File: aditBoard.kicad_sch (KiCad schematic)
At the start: 36 parts, among them J1 USB_C_Receptacle_USB2.0, J2 Hashboard0, U2 W25X40CLUXIG TR, U3 RP2040, U4 RT9080-33GJ5, Y1 12MHz

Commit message: pretty much routed
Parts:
- removed R24, R26, R28: 4.7K, Resistor_SMD:R_0805_2012Metric, symbol Device:R_US
- added R1: 10k, Resistor_SMD:R_0402_1005Metric, symbol Device:R_US
- J2: footprint Connector_PinHeader_2.00mm:PinHeader_2x09_P2.00mm_Horizontal -> aditBoard:PinHeader_2x09_P2.00mm_Horizontal
- R25, R27, R29: footprint Resistor_SMD:R_0805_2012Metric -> Resistor_SMD:R_0402_1005Metric
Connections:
- net PLUG0 is gone; now on net PLUG: J2.5 (Pin_5)
- net RST0 is gone; now on net RST: J2.15 (Pin_15)
- net SCL0 is gone; now on net SCL: J2.4 (Pin_4)
- net SDA0 is gone; now on net SDA: J2.3 (Pin_3)
- net UART_RX is gone; now on net RXD: U3.12 (GPIO9)
- net UART_TX is gone; now on net TXD: U3.11 (GPIO8)
- net 3V3: now also R1.1
- net QSPI_SS: now also R1.2
- net PLUG: now reaches U3.13 (GPIO10)
- net RST: now reaches U3.14 (GPIO11)
- net A00 renamed A0
- net A10 renamed A1
- net A20 renamed A2
- net I2C_SCL renamed SCL
- net I2C_SDA renamed SDA
- net POWERUP: no longer names the net of U3.8 (GPIO6)
- net RXD0 renamed RXD
- net TXD0 renamed TXD
- no-connect marks 14 -> 28
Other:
- moved on the sheet: R27, R29, TP1, TP6

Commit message: added artwork, DRC, LCSC BOM
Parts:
- removed TP1, TP4, TP5, TP6: TestPoint, TestPoint:TestPoint_Pad_D1.0mm, symbol Connector:TestPoint
- C17, C18: LCSC Part (none) -> C52923
- J1: LCSC Part (none) -> C2988369
- J2: LCSC C3012192 -> (none); LCSC Part (none) -> C3012192
- R1: LCSC Part (none) -> C25744
- R25, R27, R29: LCSC Part (none) -> C25900
- R4, R5: LCSC Part (none) -> C25905
- U3: LCSC Part (none) -> C2040
- U4: value RT9080-33GJ5 -> AP2112K-3.3TRG1; footprint aditBoard:RT9080-33GJ5 -> aditBoard:SOT-25-5_L2.9-W1.6-P0.95-LS2.8-BL; symbol aditBoard:RT9080-33GJ5 -> aditBoard:AP2112K-3.3TRG1; DK 1028-1509-1-ND -> (none); LCSC Part (none) -> C51118; PARTNO RT9080-33GJ5 -> (none)
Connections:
- net SWCLK: now reaches U3.24 (SWCLK)
- net SWCLK: now also J1.A8 (SBU1)
- net SWD: now reaches U3.25 (SWD)
- net SWD: now also J1.B8 (SBU2)
- no-connect marks 28 -> 26

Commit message: add readme
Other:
- title: (none) -> aditBoard
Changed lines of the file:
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@@
 	(generator_version "8.0")
 	(paper "A4")
+	(title_block
+		(title "aditBoard")
+		(date "2024-03-26")
+		(rev "1")
+	)
 	(junction
 		(at 204.47 29.21)

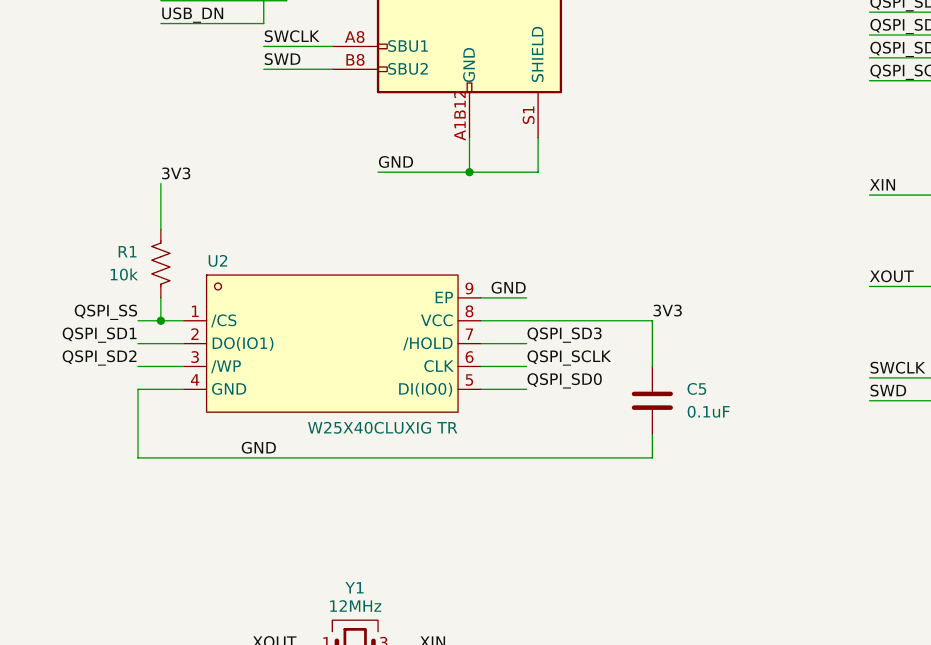
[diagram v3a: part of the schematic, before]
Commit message: Switched SPI Flash part number for #1
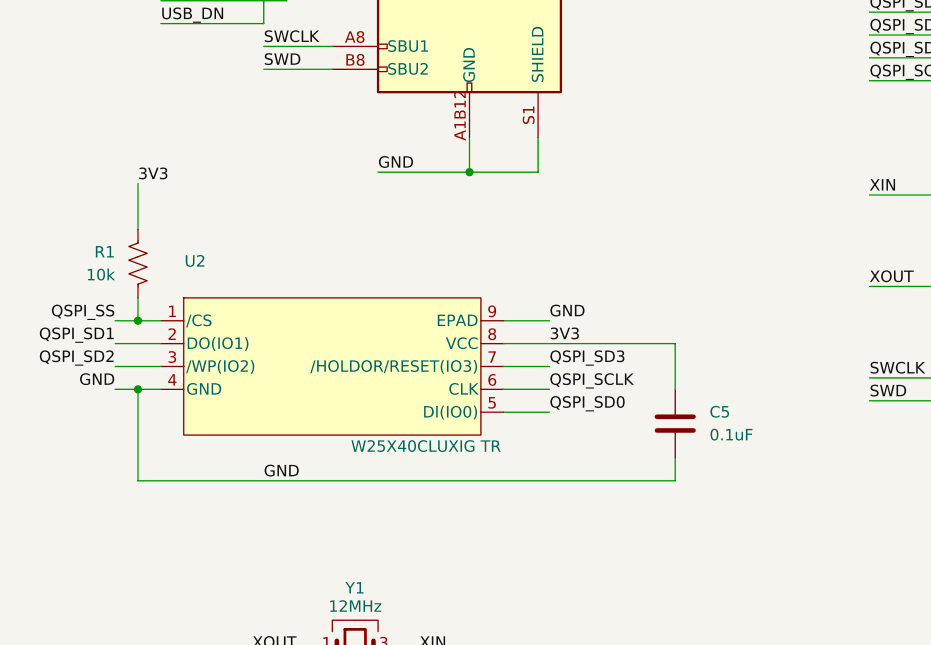
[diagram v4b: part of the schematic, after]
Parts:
- R1: PARTNO (none) -> 0402WGF1002TCE
- U2: symbol aditBoard:W25X40CLUXIGTR -> aditBoard:W25Q16JVUXIQ_TR; DK (none) -> 256-W25Q16JVUXIQTRCT-ND; LCSC (none) -> C2843335; PARTNO (none) -> W25Q16JVUXIQ TR
- U3: PARTNO (none) -> RP2040
- U4: PARTNO (none) -> AP2112K-3.3TRG1
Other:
- moved on the sheet: C5, R1
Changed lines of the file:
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@@
 	)
 	(junction
+		(at 31.75 133.35)
+		(diameter 0)
+		(color 0 0 0 0)
+	)
+	(junction
 		(at 204.47 39.37)
 		(diameter 0)
@@
 	)
 	(junction
-		(at 34.29 125.73)
+		(at 31.75 125.73)
 		(diameter 0)
 		(color 0 0 0 0)
@@
 	(wire
 		(pts
-			(xy 88.9 140.97) (xy 31.75 140.97)
+			(xy 91.44 143.51) (xy 31.75 143.51)
 		)
 		(stroke
@@
 	(wire
 		(pts
-			(xy 69.85 133.35) (xy 74.93 133.35)
+			(xy 72.39 135.89) (xy 77.47 135.89)
 		)
 		(stroke
@@
 	(wire
 		(pts
-			(xy 69.85 130.81) (xy 74.93 130.81)
+			(xy 72.39 133.35) (xy 77.47 133.35)
 		)
 		(stroke
@@
 	(wire
 		(pts
-			(xy 31.75 140.97) (xy 31.75 133.35)
+			(xy 31.75 143.51) (xy 31.75 133.35)
 		)
 		(stroke
@@
 	(wire
 		(pts
-			(xy 34.29 123.19) (xy 34.29 125.73)
+			(xy 31.75 123.19) (xy 31.75 125.73)
 		)
 		(stroke
@@
 	(wire
 		(pts
-			(xy 69.85 123.19) (xy 74.93 123.19)
+			(xy 72.39 125.73) (xy 77.47 125.73)
 		)
 		(stroke
@@
 	(wire
 		(pts
-			(xy 31.75 130.81) (xy 36.83 130.81)
+			(xy 29.21 130.81) (xy 34.29 130.81)
 		)
 		(stroke
@@
 	(wire
 		(pts
-			(xy 34.29 125.73) (xy 36.83 125.73)
+			(xy 31.75 125.73) (xy 34.29 125.73)
 		)
 		(stroke
@@
 	(wire
 		(pts
-			(xy 88.9 125.73) (xy 88.9 130.81)
+			(xy 91.44 128.27) (xy 91.44 133.35)
 		)
 		(stroke
@@
 	(wire
 		(pts
-			(xy 34.29 110.49) (xy 34.29 115.57)
+			(xy 31.75 110.49) (xy 31.75 115.57)
 		)
 		(stroke
@@
 	(wire
 		(pts
-			(xy 31.75 128.27) (xy 36.83 128.27)
+			(xy 29.21 128.27) (xy 34.29 128.27)
 		)
 		(stroke
@@
 	(wire
 		(pts
-			(xy 31.75 125.73) (xy 34.29 125.73)
+			(xy 29.21 125.73) (xy 31.75 125.73)
 		)
 		(stroke
@@
 	(wire
 		(pts
-			(xy 69.85 128.27) (xy 74.93 128.27)
+			(xy 72.39 130.81) (xy 77.47 130.81)
 		)
 		(stroke
@@
 	(wire
 		(pts
-			(xy 69.85 125.73) (xy 88.9 125.73)
+			(xy 72.39 128.27) (xy 91.44 128.27)
 		)
 		(stroke
@@
 	(wire
 		(pts
-			(xy 31.75 133.35) (xy 36.83 133.35)
+			(xy 29.21 133.35) (xy 31.75 133.35)
 		)
 		(stroke
@@
 	(wire
 		(pts
+			(xy 31.75 133.35) (xy 34.29 133.35)
+		)
+		(stroke
+			(width 0)
+			(type default)
+		)
+	)
+	(wire
+		(pts
 			(xy 74.93 43.18) (xy 74.93 46.99)
 		)
@@
 	(wire
 		(pts
-			(xy 88.9 138.43) (xy 88.9 140.97)
+			(xy 91.44 140.97) (xy 91.44 143.51)
 		)
 		(stroke
@@
 	)
 	(label "QSPI_SD2"
-		(at 31.75 130.81 180)
+		(at 29.21 130.81 180)
 		(fields_autoplaced yes)
 		(effects
@@
 	)
 	(label "QSPI_SD0"
-		(at 74.93 133.35 0)
+		(at 77.47 135.89 0)
 		(fields_autoplaced yes)
 		(effects
@@
 	)
 	(label "QSPI_SD1"
-		(at 31.75 128.27 180)
+		(at 29.21 128.27 180)
 		(fields_autoplaced yes)
 		(effects
@@
 	)
 	(label "QSPI_SD3"
-		(at 74.93 128.27 0)
+		(at 77.47 130.81 0)
 		(fields_autoplaced yes)
 		(effects
@@
 	)
 	(label "QSPI_SCLK"
-		(at 74.93 130.81 0)
+		(at 77.47 133.35 0)
 		(fields_autoplaced yes)
 		(effects
@@
 	)
 	(label "3V3"
-		(at 34.29 110.49 0)
+		(at 31.75 110.49 0)
 		(fields_autoplaced yes)
 		(effects
@@
 	)
 	(label "QSPI_SS"
-		(at 31.75 125.73 180)
+		(at 29.21 125.73 180)
 		(fields_autoplaced yes)
 		(effects
@@
 	)
 	(label "GND"
-		(at 43.18 140.97 0)
+		(at 45.72 143.51 0)
 		(fields_autoplaced yes)
 		(effects
@@
 	)
 	(label "GND"
-		(at 74.93 123.19 180)
+		(at 29.21 133.35 180)
 		(fields_autoplaced yes)
 		(effects
@@
 		)
 	)
+	(label "GND"
+		(at 77.47 125.73 0)
+		(fields_autoplaced yes)
+		(effects
+			(font
+				(size 1.27 1.27)
+			)
+			(justify left bottom)
+		)
+	)
 	(label "SDA"
 		(at 184.15 101.6 180)
@@
 	)
 	(label "3V3"
-		(at 88.9 125.73 0)
+		(at 77.47 128.27 0)
 		(fields_autoplaced yes)
 		(effects
@@
 	(symbol
 		(lib_id "Device:R_US")
-		(at 34.29 119.38 0)
+		(at 31.75 119.38 0)
 		(mirror y)
 		(unit 1)
@@
 		(dnp no)
 		(property "Reference" "R1"
-			(at 31.75 118.1099 0)
+			(at 29.21 118.1099 0)
 			(effects
 				(font
@@
 		)
 		(property "Value" "10k"
-			(at 31.75 120.6499 0)
+			(at 29.21 120.6499 0)
 			(effects
 				(font
@@
 		)
 		(property "Footprint" "Resistor_SMD:R_0402_1005Metric"
-			(at 33.274 119.634 90)
+			(at 30.734 119.634 90)
 			(effects
 				(font
@@
 		)
 		(property "Datasheet" "~"
-			(at 34.29 119.38 0)
+			(at 31.75 119.38 0)
 			(effects
 				(font
@@
 		)
 		(property "Description" "Resistor, US symbol"
-			(at 34.29 119.38 0)
+			(at 31.75 119.38 0)
 			(effects
 				(font
@@
 		)
 		(property "LCSC Part" "C25744"
-			(at 34.29 119.38 0)
+			(at 31.75 119.38 0)
+			(effects
+				(font
+					(size 1.27 1.27)
+				)
+				(hide yes)
+			)
+		)
+		(property "PARTNO" "0402WGF1002TCE"
+			(at 31.75 119.38 0)
 			(effects
 				(font
@@
 			)
 		)
-		(property "PARTNO" ""
+		(property "PARTNO" "AP2112K-3.3TRG1"
 			(at 57.15 34.29 0)
 			(effects
@@
 			)
 		)
+		(property "PARTNO" "RP2040"
+			(at 151.13 104.14 0)
+			(effects
+				(font
+					(size 1.27 1.27)
+				)
+				(hide yes)
+			)
+		)
 		(pin "1"
 		)
@@
 	(symbol
 		(lib_id "Device:C")
-		(at 88.9 134.62 180)
+		(at 91.44 137.16 180)
 		(unit 1)
 		(exclude_from_sim no)
@@
 		(fields_autoplaced yes)
 		(property "Reference" "C5"
-			(at 92.71 133.3499 0)
+			(at 95.25 135.8899 0)
 			(effects
 				(font
@@
 		)
 		(property "Value" "0.1uF"
-			(at 92.71 135.8899 0)
+			(at 95.25 138.4299 0)
 			(effects
 				(font
@@
 		)
 		(property "Footprint" "Capacitor_SMD:C_0402_1005Metric"
-			(at 88.9 127 0)
+			(at 91.44 129.54 0)
 			(effects
 				(font
@@
 		)
 		(property "Datasheet" ""
-			(at 88.9 124.46 0)
+			(at 91.44 127 0)
 			(effects
 				(font
@@
 		)
 		(property "Description" ""
-			(at 88.9 134.62 0)
+			(at 91.44 137.16 0)
 			(effects
 				(font
@@
 		)
 		(property "Manufacturer" "SAMSUNG(三星)"
-			(at 88.9 121.92 0)
+			(at 91.44 124.46 0)
 			(effects
 				(font
@@
 		)
 		(property "LCSC Part" "C307331"
-			(at 88.9 119.38 0)
+			(at 91.44 121.92 0)
 			(effects
 				(font
@@
 		)
 		(property "JLC Part" "Basic Part"
-			(at 88.9 116.84 0)
+			(at 91.44 119.38 0)
 			(effects
 				(font
@@
 		)
 		(property "PARTNO" "CL05B104KB54PNC"
-			(at 88.9 134.62 0)
+			(at 91.44 137.16 0)
 			(effects
 				(font
@@
 	)
 	(symbol
-		(lib_id "aditBoard:W25X40CLUXIGTR")
+		(lib_id "aditBoard:W25Q16JVUXIQ_TR")
 		(at 53.34 129.54 0)
 		(unit 1)
@@
 		(dnp no)
 		(property "Reference" "U2"
-			(at 40.64 119.126 0)
+			(at 38.1 119.126 0)
 			(effects
 				(font
@@
 		)
 		(property "Value" "W25X40CLUXIG TR"
-			(at 58.928 137.668 0)
+			(at 63.754 139.7 0)
 			(effects
 				(font
@@
 			)
 		)
-		(property "Datasheet" "https://lcsc.com/product-detail/FLASH_Winbond-Elec-W25X40CLUXIG-TR_C401661.html"
-			(at 53.34 143.51 0)
+		(property "Datasheet" "W25Q16JVUXIQ TR"
+			(at 53.594 146.304 0)
 			(effects
 				(font
 					(size 1.27 1.27)
+					(italic yes)
 				)
 				(hide yes)
@@
 		)
 		(property "Description" ""
-			(at 53.34 129.54 0)
+			(at 35.56 124.46 0)
 			(effects
 				(font
@@
 			(effects
 				(font
+					(size 1.27 1.27)
+				)
+				(hide yes)
+			)
+		)
+		(property "DK" "256-W25Q16JVUXIQTRCT-ND"
+			(at 54.102 149.352 0)
+			(effects
+				(font
+					(size 1.27 1.27)
+				)
+				(hide yes)
+			)
+		)
+		(property "PARTNO" "W25Q16JVUXIQ TR"
+			(at 54.61 151.638 0)
+			(effects
+				(font
+					(size 1.27 1.27)
+				)
+				(hide yes)
+			)
+		)
+		(property "LCSC" "C2843335"
+			(at 54.102 154.178 0)
+			(effects
+				(font

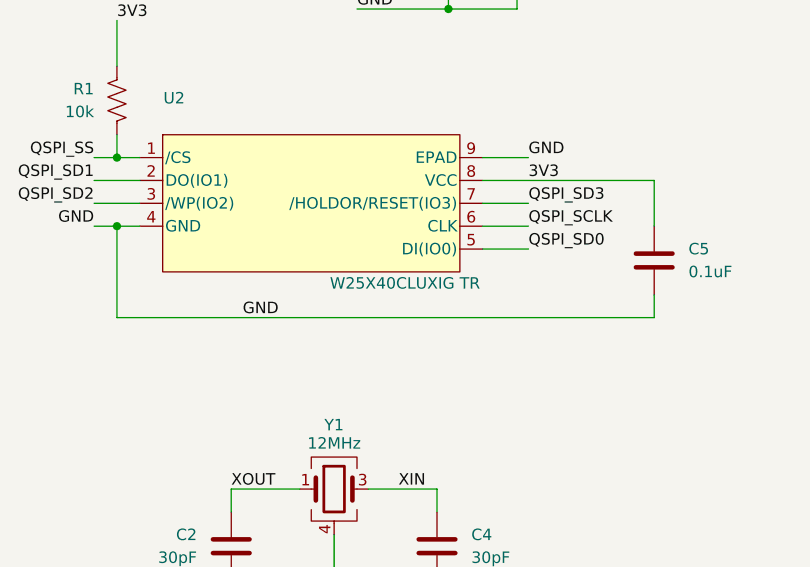
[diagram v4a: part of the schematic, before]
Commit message: updated render to reflect the correct side for soldering the data connector.
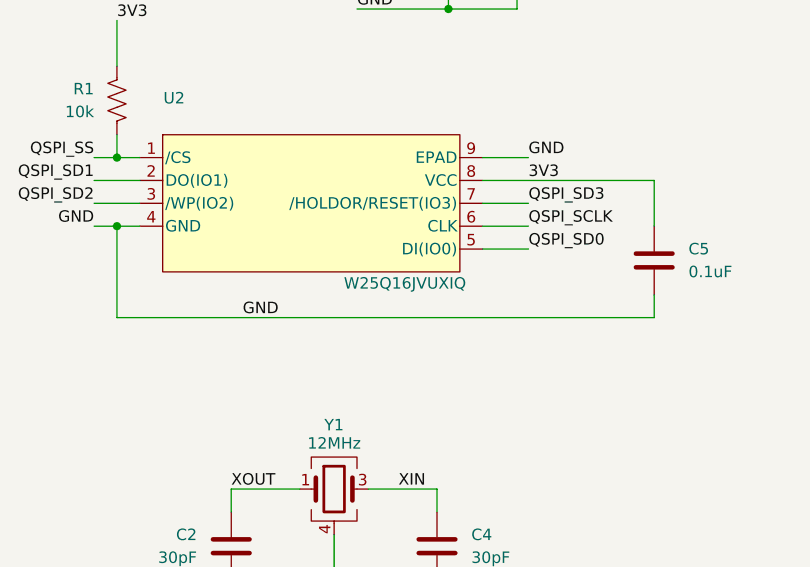
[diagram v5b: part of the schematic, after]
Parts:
- U2: value W25X40CLUXIG TR -> W25Q16JVUXIQ; JLC Part Extended Part -> (none); LCSC Part C401661 -> (none); Manufacturer WINBOND(华邦) -> (none); PARTNO W25Q16JVUXIQ TR -> W25Q16JVUXIQ
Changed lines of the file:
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@@
 			)
 		)
-		(property "Value" "W25X40CLUXIG TR"
+		(property "Value" "W25Q16JVUXIQ"
 			(at 63.754 139.7 0)
 			(effects
@@
 			)
 		)
-		(property "Datasheet" "W25Q16JVUXIQ TR"
+		(property "Datasheet" "https://www.winbond.com/resource-files/w25q16jv%20spi%20revh%2004082019%20plus.pdf"
 			(at 53.594 146.304 0)
 			(effects
@@
 			)
 		)
-		(property "Manufacturer" "WINBOND(华邦)"
-			(at 53.34 146.05 0)
-			(effects
-				(font
-					(size 1.27 1.27)
-				)
-				(hide yes)
-			)
-		)
-		(property "LCSC Part" "C401661"
-			(at 53.34 148.59 0)
-			(effects
-				(font
-					(size 1.27 1.27)
-				)
-				(hide yes)
-			)
-		)
-		(property "JLC Part" "Extended Part"
-			(at 53.34 151.13 0)
-			(effects
-				(font
-					(size 1.27 1.27)
-				)
-				(hide yes)
-			)
-		)
 		(property "DK" "256-W25Q16JVUXIQTRCT-ND"
 			(at 54.102 149.352 0)
@@
 			)
 		)
-		(property "PARTNO" "W25Q16JVUXIQ TR"
+		(property "PARTNO" "W25Q16JVUXIQ"
 			(at 54.61 151.638 0)
 			(effects
